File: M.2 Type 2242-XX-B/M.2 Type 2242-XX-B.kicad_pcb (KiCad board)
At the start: 4 copper layers, 30 x 42 mm, 86 parts, among them J101 ANT1, J102 ANT2, M201 MountingHole_Pad, U201 STM32F103C8Tx, U301 M.2_NGFF_Socket2_KeyB_SSIC_Ad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, U401 AS193-73, U402 M74VHC1GT04DFT1G, U403 ADF7021BCPZ, X401 FT5HNBPK19.44-T1, Y201 12MHz

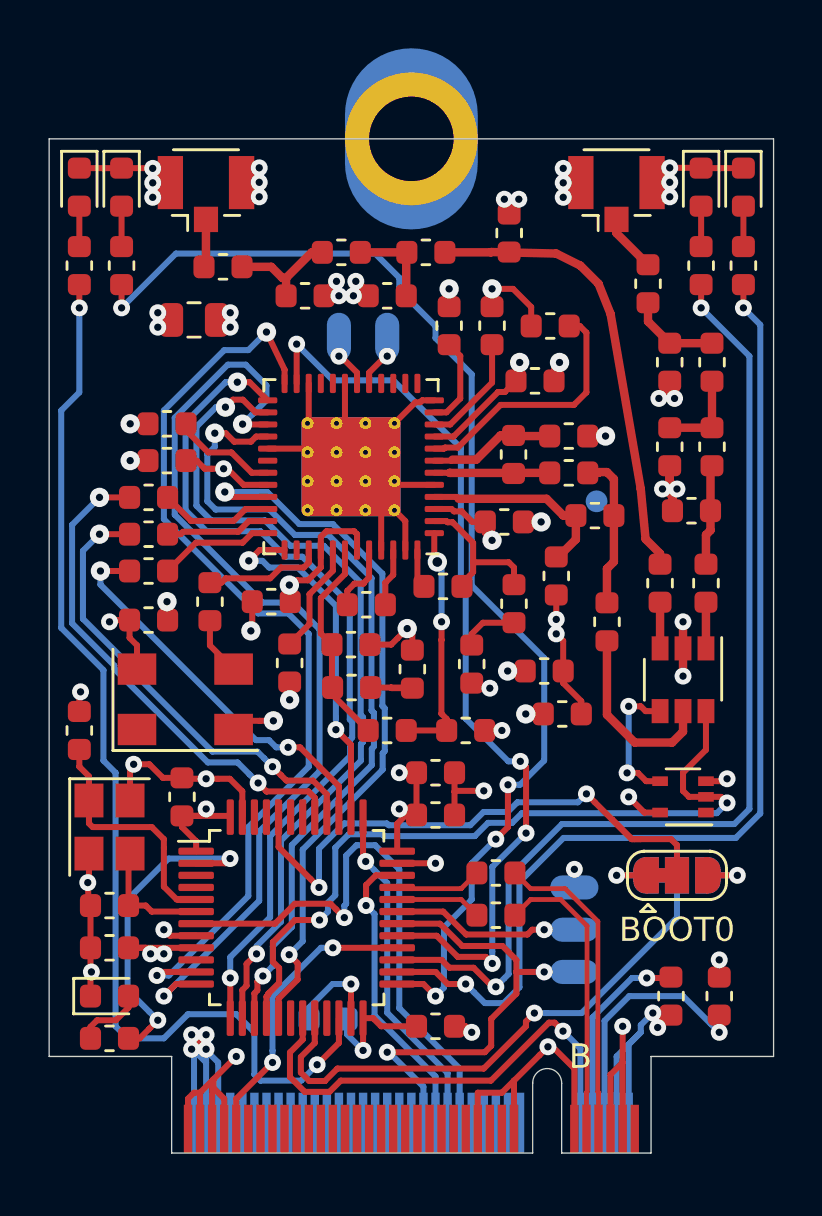
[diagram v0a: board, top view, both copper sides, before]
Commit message: Add project named, data and antenna numbers
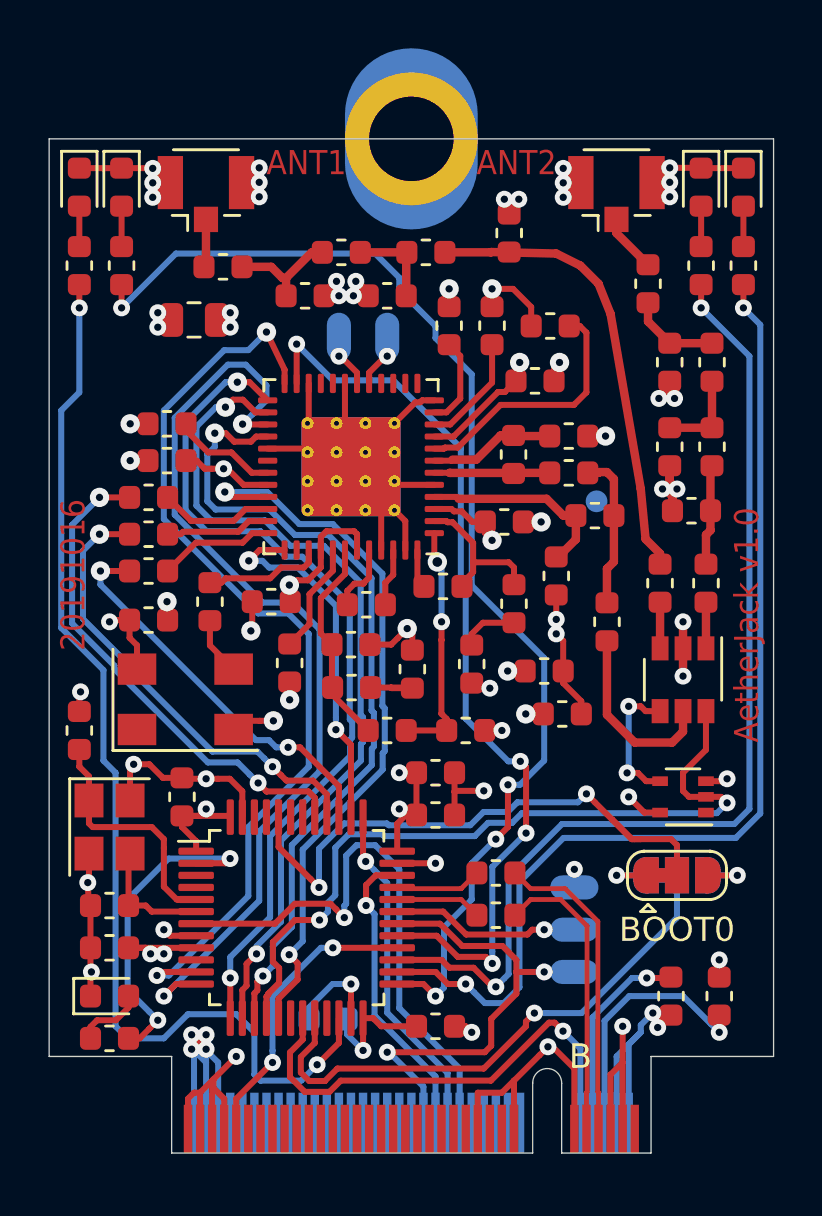
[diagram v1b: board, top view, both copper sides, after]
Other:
- board text added: "20191016"
- board text added: "ANT1"
- board text added: "ANT2"
- board text added: "AetherJack v1.0"
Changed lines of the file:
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@@
   (general
     (thickness 0.8)
-    (drawings 28)
+    (drawings 36)
     (tracks 1085)
     (zones 0)
@@
     (37 F.SilkS user)
     (38 B.Mask user hide)
-    (39 F.Mask user hide)
+    (39 F.Mask user)
     (40 Dwgs.User user)
     (41 Cmts.User user)
@@
     )
   )
+  (gr_text ANT2 (at 13.7 1) (layer F.Cu)
+    (effects (font (size 1 0.9) (thickness 0.15)) (justify left))
+  )
+  (gr_text ANT2 (at 13.7 1) (layer F.Mask)
+    (effects (font (size 1 0.9) (thickness 0.15)) (justify left))
+  )
+  (gr_text ANT1 (at 5 1) (layer F.Mask)
+    (effects (font (size 1 0.9) (thickness 0.15)) (justify left))
+  )
+  (gr_text ANT1 (at 5 1) (layer F.Cu)
+    (effects (font (size 1 0.9) (thickness 0.15)) (justify left))
+  )
+  (gr_text 20191016 (at -3 21.2 90) (layer F.Mask)
+    (effects (font (size 1 0.9) (thickness 0.15)) (justify left))
+  )
+  (gr_text 20191016 (at -3 21.2 90) (layer F.Cu)
+    (effects (font (size 1 0.9) (thickness 0.15)) (justify left))
+  )
+  (gr_text "AetherJack v1.0" (at 24.9 25 90) (layer F.Mask)
+    (effects (font (size 1 0.9) (thickness 0.15)) (justify left))
+  )
+  (gr_text "AetherJack v1.0" (at 24.9 25 90) (layer F.Cu)
+    (effects (font (size 1 0.9) (thickness 0.15)) (justify left))
+  )
   (gr_text "Board thickness should be 0.8 mm!\nIf this was not selected when ordering, STOP, and turn back to customer." (at 145.75 147) (layer Cmts.User)

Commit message: Add rounded corners
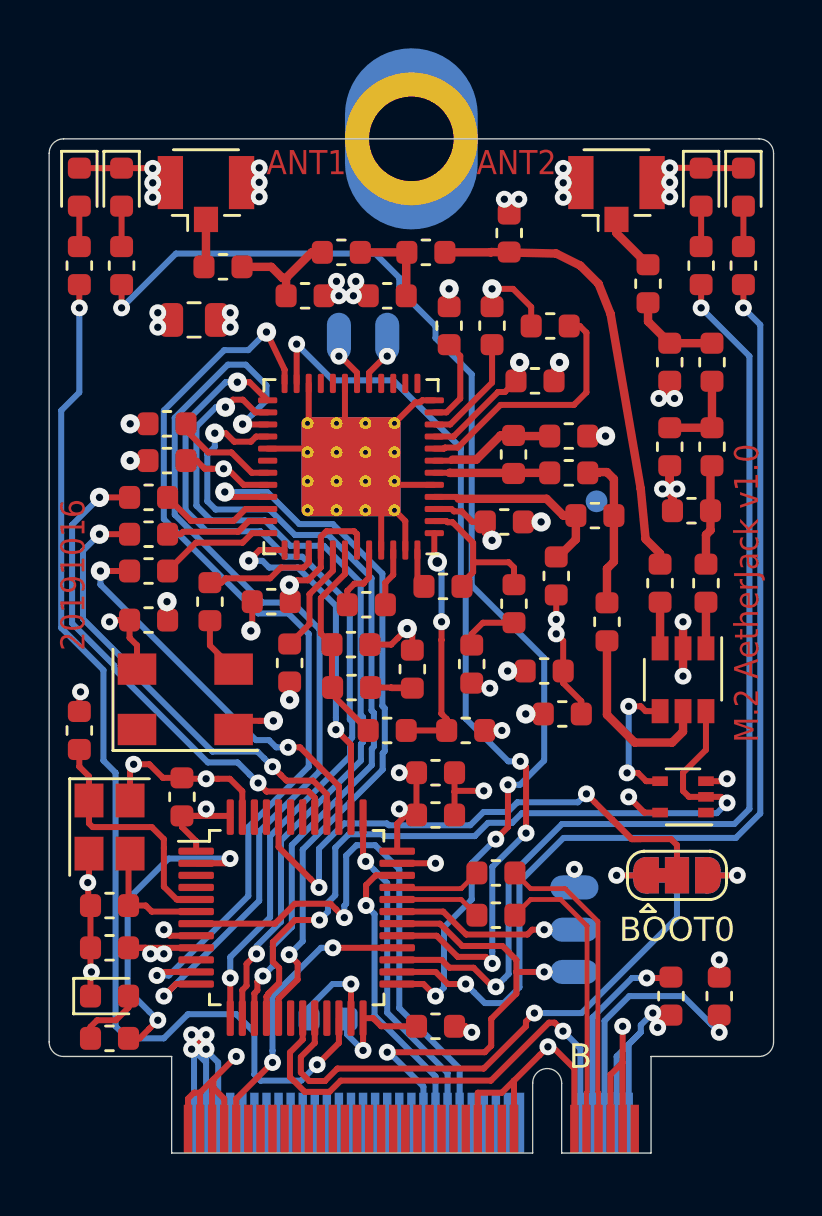
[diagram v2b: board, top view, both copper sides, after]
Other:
- outline, holes or cut-outs redrawn
- board text added: "M.2 AetherJack v1.0"
- board text removed: "AetherJack v1.0"
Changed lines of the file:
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@@
   (general
     (thickness 0.8)
-    (drawings 36)
+    (drawings 40)
     (tracks 1085)
     (zones 0)
@@
   (page A4)
   (title_block
-    (title "M.2 Type 2242-XX-B")
+    (title AetherJack)
+    (rev v1.1)
   )
   (layers
@@
       (layerselection 0x010fc_ffffffff)
       (usegerberextensions false)
-      (usegerberattributes false)
+      (usegerberattributes true)
       (usegerberadvancedattributes false)
-      (creategerberjobfile false)
+      (creategerberjobfile true)
       (excludeedgelayer true)
       (linewidth 0.100000)
@@
     )
   )
+  (gr_arc (start -3.4 37.4) (end -4 37.4) (angle -90) (layer Edge.Cuts) (width 0.05))
+  (gr_arc (start 25.4 37.4) (end 25.4 38) (angle -90) (layer Edge.Cuts) (width 0.05))
+  (gr_arc (start 25.4 0.6) (end 26 0.6) (angle -90) (layer Edge.Cuts) (width 0.05))
+  (gr_arc (start -3.4 0.6) (end -3.4 0) (angle -90) (layer Edge.Cuts) (width 0.05))
   (gr_text ANT2 (at 13.7 1) (layer F.Cu)
     (effects (font (size 1 0.9) (thickness 0.15)) (justify left))
@@
     (effects (font (size 1 0.9) (thickness 0.15)) (justify left))
   )
-  (gr_text "AetherJack v1.0" (at 24.9 25 90) (layer F.Mask)
+  (gr_text "M.2 AetherJack v1.0" (at 24.9 25 90) (layer F.Mask)
     (effects (font (size 1 0.9) (thickness 0.15)) (justify left))
   )
-  (gr_text "AetherJack v1.0" (at 24.9 25 90) (layer F.Cu)
+  (gr_text "M.2 AetherJack v1.0" (at 24.9 25 90) (layer F.Cu)
     (effects (font (size 1 0.9) (thickness 0.15)) (justify left))
   )
@@
   (gr_line (start 16.025 39.1) (end 16.025 42) (layer Edge.Cuts) (width 0.05))
   (gr_arc (start 16.625 39.1) (end 17.225 39.1) (angle -180) (layer Edge.Cuts) (width 0.05))
-  (gr_line (start 26 38) (end 20.925 38) (layer Edge.Cuts) (width 0.05))
-  (gr_line (start -4 38) (end 1.075 38) (layer Edge.Cuts) (width 0.05))
-  (gr_line (start -4 0) (end -4 38) (layer Edge.Cuts) (width 0.05))
+  (gr_line (start 25.4 38) (end 20.925 38) (layer Edge.Cuts) (width 0.05))
+  (gr_line (start -3.4 38) (end 1.075 38) (layer Edge.Cuts) (width 0.05))
+  (gr_line (start -4 0.6) (end -4 37.4) (layer Edge.Cuts) (width 0.05))
   (gr_line (start 1.075 42) (end 16.025 42) (layer Edge.Cuts) (width 0.05))
   (gr_line (start 20.925 42) (end 20.925 38) (layer Edge.Cuts) (width 0.05))
   (gr_line (start 1.075 42) (end 1.075 38) (layer Edge.Cuts) (width 0.05))
-  (gr_line (start 26 0) (end 26 38) (layer Edge.Cuts) (width 0.05))
-  (gr_line (start -4 0) (end 26 0) (layer Edge.Cuts) (width 0.05))
+  (gr_line (start 26 0.6) (end 26 37.4) (layer Edge.Cuts) (width 0.05))
+  (gr_line (start -3.4 0) (end 25.4 0) (layer Edge.Cuts) (width 0.05))
   (gr_text "Finger keeoput on bottom" (at 26.5 36.5) (layer B.Fab)
     (effects (font (size 1 1) (thickness 0.15)) (justify left))

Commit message: Fix DRC error with ANT1/2 in copper
Add solder mask removal for RF traces
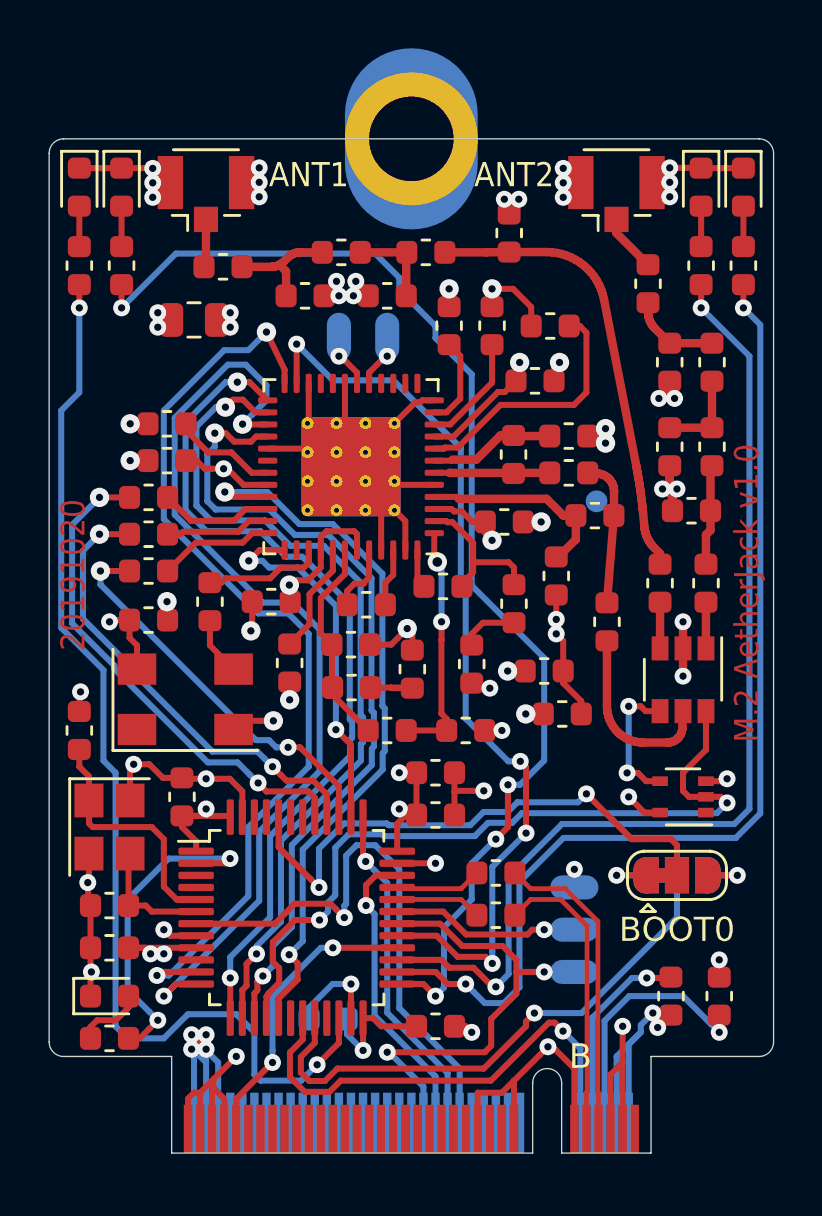
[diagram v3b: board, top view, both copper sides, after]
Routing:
- net GND: track 131.6 -> 132.4 mm, vias 59 -> 60
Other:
- board text added: "20191020"
- board text removed: "20191016"

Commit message: Adjust my nickname
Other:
- board text added: "nickoe"
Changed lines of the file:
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@@
   (general
     (thickness 0.8)
-    (drawings 223)
+    (drawings 224)
     (tracks 1220)
     (zones 0)
@@
   )
   (setup
-    (last_trace_width 0.35)
+    (last_trace_width 0.25)
     (user_trace_width 0.35)
     (trace_clearance 0.2)
@@
     )
   )
+  (gr_text nickoe (at -2.6 27.9 270) (layer B.Cu)
+    (effects (font (size 1 0.9) (thickness 0.15)) (justify mirror))
+  )
   (gr_line (start 14.6923 12.2825) (end 13.6906 13.2842) (layer F.Mask) (width 0.75))
